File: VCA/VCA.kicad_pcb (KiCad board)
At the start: 2 copper layers, 36 parts, among them J1 Output, J2 Input, J3 Power, J4 Env, Q1 BC817, Q2 BC817, Q3 BC817, Q4 BC817, Q5 BC807, U1 LM324

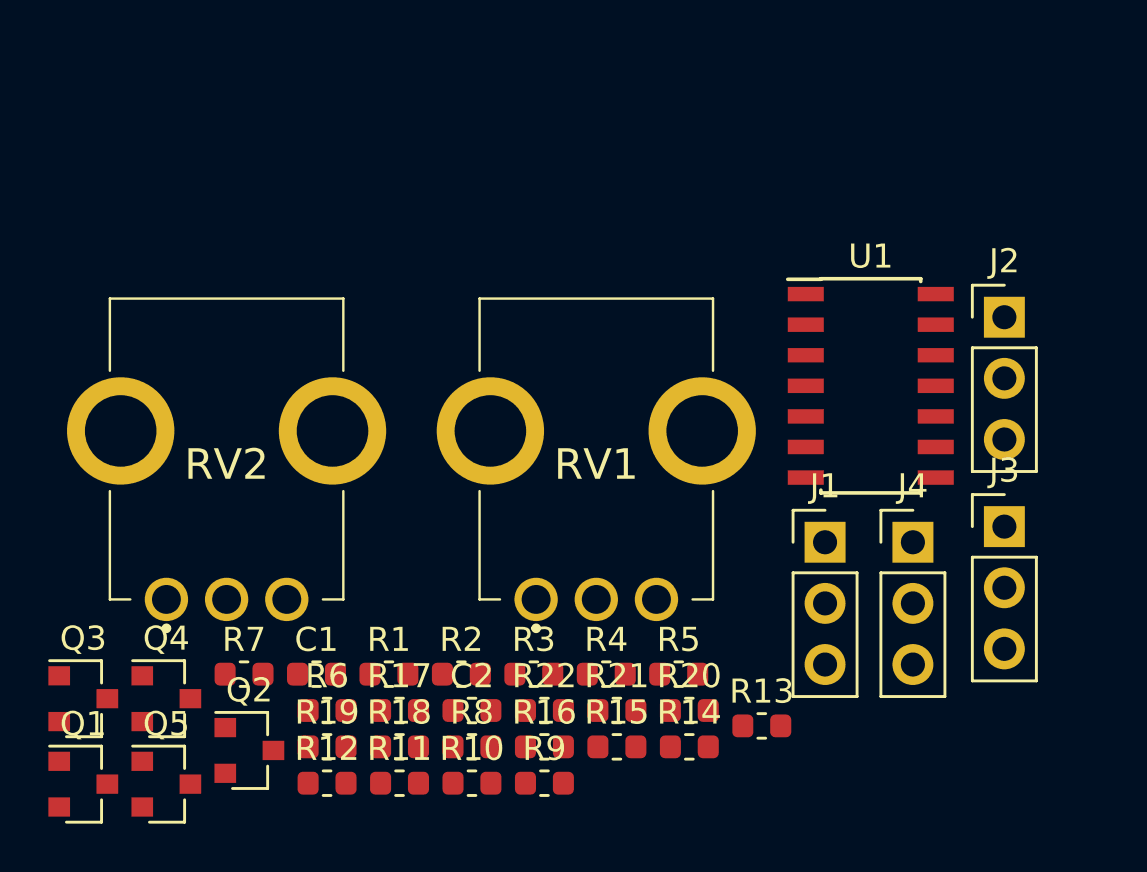
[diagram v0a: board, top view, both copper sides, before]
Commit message: Изменены библиотеки. Добавлинны библиотеки примененные в проекте локально. Добавленны заготовки для печатных плат. Добавленны 3D модели компоненток.
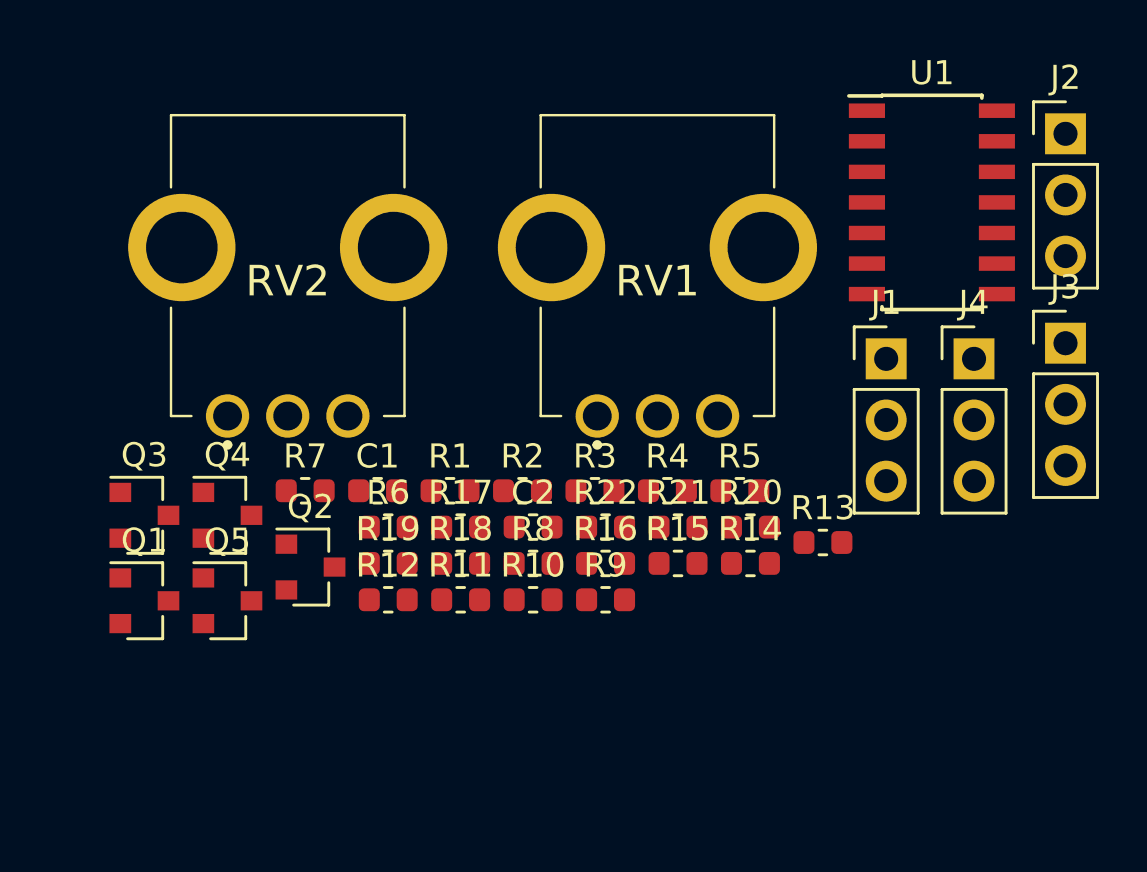
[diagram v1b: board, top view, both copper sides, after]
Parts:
- C1, C2: footprint Capacitor_SMD:C_0603_1608Metric -> footprint:c0603
- J1, J2, J3, J4: footprint Connector_PinHeader_2.54mm:PinHeader_1x03_P2.54mm_Vertical -> footprint:pls1x03
- Q1, Q2, Q3, Q4, Q5: footprint Package_TO_SOT_SMD:SOT-23 -> footprint:SOT-23
- R1, R10, R11, R12, R13, R14, R15, R16, R17, R18, R19, R2, R20, R21, R22, R3, R4, R5, R6, R7, R8, R9: footprint Resistor_SMD:R_0603_1608Metric -> footprint:r0603
- RV1, RV2: footprint R0409N:PTV09A4020FB103 -> footprint:PTV09A4020FB103
- U1: footprint Package_SO:SOIC-14_3.9x8.7mm_P1.27mm -> footprint:soic-14
- moved J1 8.03 mm to (151.9, 82.3)
- moved R13 8.03 mm to (149.3, 89.9)
- moved R16 8.03 mm to (140.3, 90.8)
- moved R19 8.03 mm to (131.2, 90.8)
- moved R22 8.03 mm to (140.3, 89.3)
- moved R6 8.03 mm to (131.2, 89.3)
- moved Q1 8.03 mm to (121.1, 92.3)
- moved Q3 8.03 mm to (121.1, 88.8)
- moved Q4 8.03 mm to (124.6, 88.8)
- moved Q5 8.03 mm to (124.6, 92.3)
- moved C2 8.03 mm to (137.3, 89.3)
- moved J3 8.03 mm to (159.4, 81.6)
- moved J4 8.03 mm to (155.6, 82.3)
- moved R14 8.03 mm to (146.3, 90.8)
- moved R15 8.03 mm to (143.3, 90.8)
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
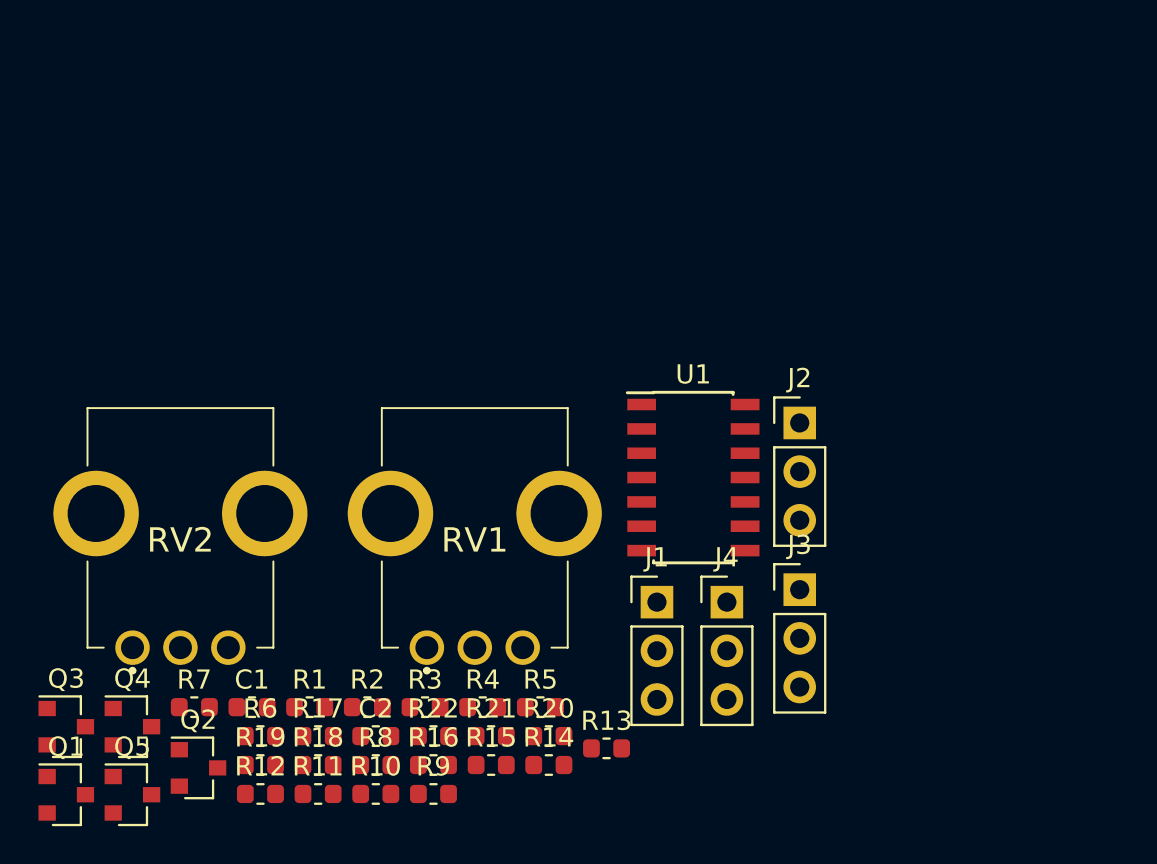
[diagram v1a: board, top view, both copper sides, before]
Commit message: Исправленну ошибки в схемах. Полностью локальные библиотеки и 3D модели.
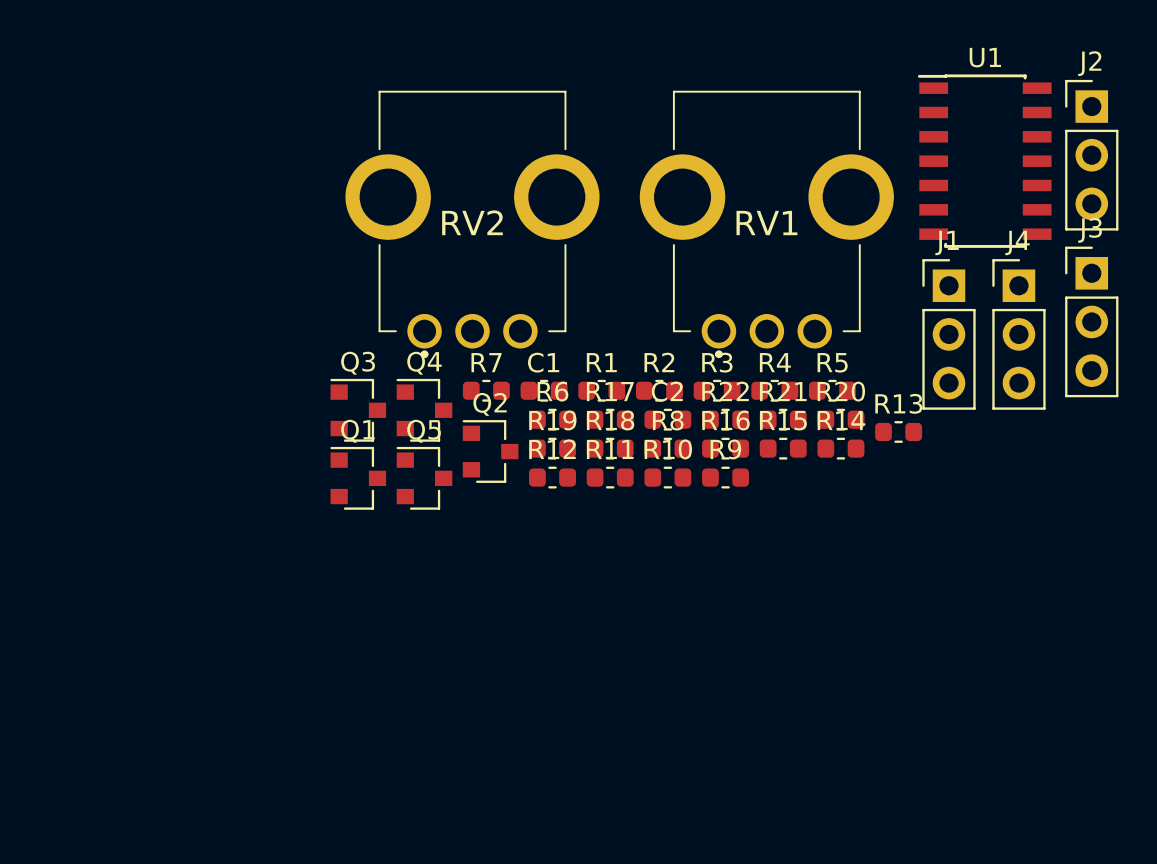
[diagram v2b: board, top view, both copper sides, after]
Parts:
- moved J2 22.5 mm to (174.6, 56.4)
- moved J4 22.5 mm to (170.8, 65.8)
- moved Q2 22.5 mm to (143.2, 74.4)
- moved Q4 22.5 mm to (139.8, 72.3)
- moved R1 22.5 mm to (149.0, 71.3)
- moved R10 22.5 mm to (152.5, 75.8)
- moved R11 22.5 mm to (149.5, 75.8)
- moved R14 22.5 mm to (161.5, 74.3)
- moved R15 22.5 mm to (158.5, 74.3)
- moved R18 22.5 mm to (149.5, 74.3)
- moved R2 22.5 mm to (152.1, 71.3)
- moved R3 22.5 mm to (155.1, 71.3)
- moved R5 22.5 mm to (161.1, 71.3)
- moved R7 22.5 mm to (143.0, 71.3)
- moved R8 22.5 mm to (152.5, 74.3)
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
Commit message: Изменение в схемах. Разведенны ПП
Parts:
- added J10: Conn_01x05_Male, footprint:pls1x05, B.Cu at (24.1, 78.0)
- added J11: Conn_01x05_Male, footprint:pls1x05, B.Cu at (73.7, 24.0)
- added J12: Conn_01x05_Male, footprint:pls1x05, B.Cu at (48.3, 24.0)
- added J5: Conn_01x05_Male, footprint:pls1x05, B.Cu at (48.3, 85.0)
- added J6: Conn_01x05_Male, footprint:pls1x05, B.Cu at (25.4, 85.0)
- added J7: Conn_01x05_Male, footprint:pls1x05, B.Cu at (72.4, 78.0)
- added J8: Conn_01x05_Male, footprint:pls1x05, B.Cu at (47.0, 78.0)
- added J9: Conn_01x05_Male, footprint:pls1x05, B.Cu at (25.4, 24.0)
- C1, C2, Q1, Q2, Q3, Q4, Q5, R1, R10, R11, R12, R13, R14, R15, R16, R17, R18, R19, R2, R20, R21, R22, R3, R4, R5, R6, R7, R8, R9, U1: moved to B.Cu
- J3: value Power -> Env
- J4: value Env -> Conn_01x05_Male; footprint footprint:pls1x03 -> footprint:pls1x05; moved to B.Cu
- RV1, RV2: footprint footprint:PTV09A4020FB103 -> footprint:R0904N
- moved J2 147.8 mm to (27.1, 47.2)
- moved J3 147.6 mm to (27.1, 60.3)
- moved R13 143.2 mm to (23.3, 49.8), turned to 180 degrees
- moved R14 140.8 mm to (23.3, 47.2), turned to 180 degrees
- moved R20 138.8 mm to (23.3, 60.3), turned to 180 degrees
- moved R21 135.6 mm to (23.3, 62.9), turned to 180 degrees
- moved R22 132.4 mm to (23.3, 65.4), turned to 180 degrees
- moved R5 132.0 mm to (31.3, 47.2), turned to 180 degrees
- moved R16 125.5 mm to (30.8, 60.3), turned to 180 degrees
- moved R12 125.4 mm to (23.3, 52.2), turned to 180 degrees
- moved R10 123.5 mm to (31.3, 52.3), turned to 180 degrees
- moved U1 123.2 mm to (45.8, 61.6), turned to 180 degrees
- moved R18 119.3 mm to (30.8, 62.8), turned to 180 degrees
- moved RV1 116.5 mm to (42.8, 42.9)
- moved R19 116.0 mm to (30.8, 65.4), turned to 180 degrees
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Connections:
- J3 pad 1: +5V -> /ENV_1
- J3 pad 2: GNDREF -> /ENV_2
- J3 pad 3: -5V -> /ENV_3
- J4 pad 1: /ENV_1 -> +5V
- J4 pad 2: /ENV_2 -> +5V
- J4 pad 3: /ENV_3 -> +5V
- U1 pad 10: Net-(RV2-Pad2) -> Net-(R16-Pad1)
- U1 pad 2: Net-(R10-Pad1) -> Net-(RV1-Pad2)
- U1 pad 3: Net-(RV1-Pad2) -> Net-(R10-Pad1)
- U1 pad 9: Net-(R16-Pad1) -> Net-(RV2-Pad2)
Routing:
- net GNDREF: track 0.00 -> 212.5 mm, vias 0 -> 1
- net -5V: track 0.00 -> 163.4 mm, vias 0 -> 1
- net +5V: track 0.00 -> 102.9 mm, vias 0 -> 2
- net Net-(R17-Pad2): track 0.00 -> 75.5 mm, vias 0 -> 1
- net Net-(Q3-Pad1): track 0.00 -> 65.0 mm, vias 0 -> 2
- net Net-(RV2-Pad2): track 0.00 -> 55.7 mm, vias 0 -> 2
- net Net-(R1-Pad1): track 0.00 -> 45.1 mm, vias 0 -> 2
- net Net-(Q2-Pad3): track 0.00 -> 38.0 mm, vias 0 -> 2
- net Net-(R10-Pad1): track 0.00 -> 28.9 mm
- net Net-(Q1-Pad3): track 0.00 -> 23.2 mm, vias 0 -> 2
- net Net-(R16-Pad1): track 0.00 -> 16.7 mm
- net Net-(RV1-Pad2): track 0.00 -> 15.2 mm
- net Net-(Q1-Pad1): track 0.00 -> 13.4 mm
- net Net-(R9-Pad2): track 0.00 -> 12.0 mm
- net Net-(Q1-Pad2): track 0.00 -> 8.10 mm
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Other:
- board outline added: 70 x 70 mm
- net class power added: clearance 0.2, trace_width 0.5, via_dia 0.8, via_drill 0.4
